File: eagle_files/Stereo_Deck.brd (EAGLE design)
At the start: 73.3 x 45.7 mm, 39 parts, among them U1 ATMEGA328P_PDIP_EZ, U2 OPA344

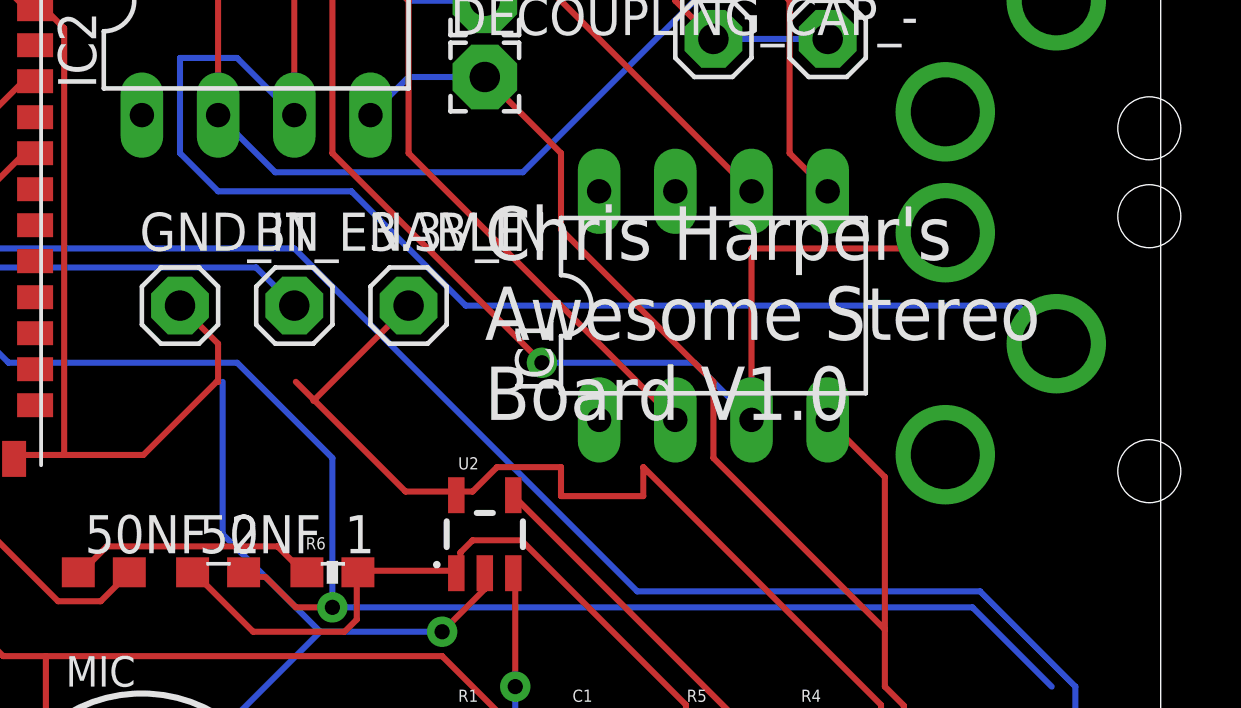
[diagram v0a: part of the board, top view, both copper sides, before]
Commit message: Updated silkscreen for new board version
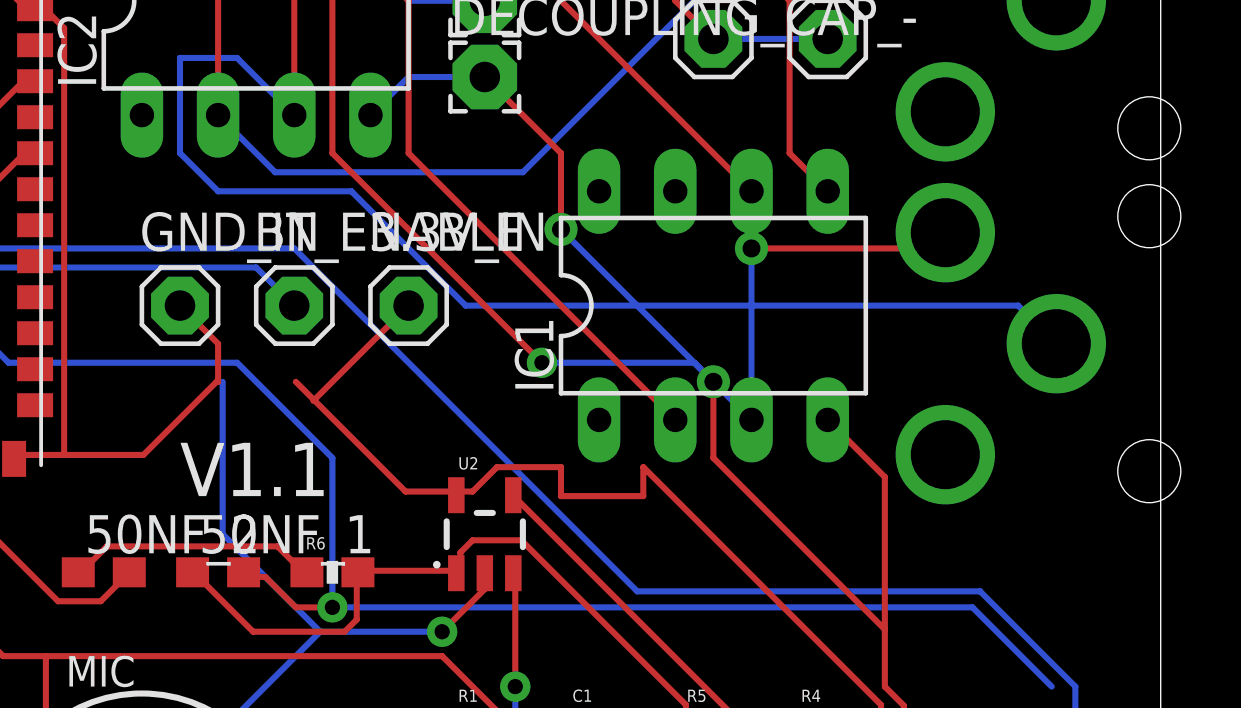
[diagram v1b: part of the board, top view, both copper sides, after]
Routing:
- net N$4: vias 1 -> 2
- net GND: vias 2 -> 4
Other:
- board text added: "V1.1"
- board text removed: "Chris Harper's Awesome Stereo Board V1.0"
